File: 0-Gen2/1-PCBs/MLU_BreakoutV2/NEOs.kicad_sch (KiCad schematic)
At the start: 36 parts

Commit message: [add] beginning routing
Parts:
- renumbered LED5 to LED1
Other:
- note added: "first two are indicators, the remaining should be on breathe mode"
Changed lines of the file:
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@@
 		)
 	)
+	(text "first two are indicators, the remaining should be on breathe mode"
+		(exclude_from_sim no)
+		(at 16.764 14.478 0)
+		(effects
+			(font
+				(size 1.27 1.27)
+			)
+			(justify left)
+		)
+	)
 	(global_label "NEO_PASS5"
 		(shape output)
@@
 		(dnp no)
 		(fields_autoplaced yes)
-		(property "Reference" "LED5"
+		(property "Reference" "LED1"
 			(at 61.976 16.764 0)
 			(effects
@@
 			)
 		)
+		(property "MFR" ""
+			(at 41.656 26.67 0)
+			(effects
+				(font
+					(size 1.27 1.27)
+				)
+				(hide yes)
+			)
+		)
+		(property "MFR S/N" ""
+			(at 41.656 26.67 0)
+			(effects
+				(font
+					(size 1.27 1.27)
+				)
+				(hide yes)
+			)
+		)
+		(property "Supplier 1" ""
+			(at 41.656 26.67 0)
+			(effects
+				(font
+					(size 1.27 1.27)
+				)
+				(hide yes)
+			)
+		)
+		(property "Supplier 1 S/N" ""
+			(at 41.656 26.67 0)
+			(effects
+				(font
+					(size 1.27 1.27)
+				)
+				(hide yes)
+			)
+		)
+		(property "Supplier 2" ""
+			(at 41.656 26.67 0)
+			(effects
+				(font
+					(size 1.27 1.27)
+				)
+				(hide yes)
+			)
+		)
+		(property "Supplier 2 S/N" ""
+			(at 41.656 26.67 0)
+			(effects
+				(font
+					(size 1.27 1.27)
+				)
+				(hide yes)
+			)
+		)
 		(pin "3"
 		)
@@
 			(project "MLU_BreakoutV2"
 				(path "/55121ba7-5d22-4fe3-93aa-7f76d75b410c/38ea1217-5551-41b6-a3b9-444cd4c6916d"
-					(reference "LED5")
+					(reference "LED1")
 					(unit 1)
 				)

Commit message: before restructure
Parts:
- renumbered LED1 to LED5

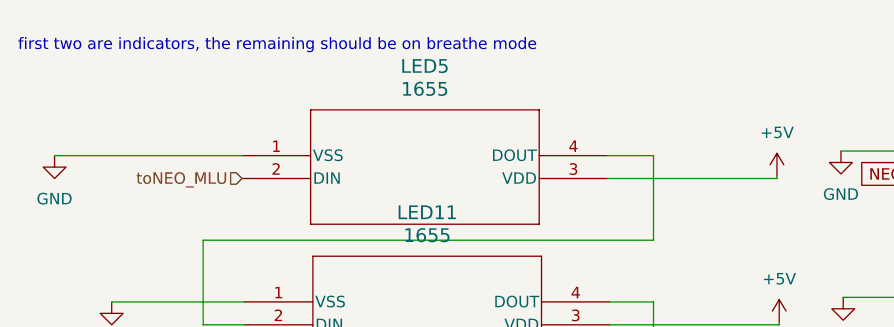
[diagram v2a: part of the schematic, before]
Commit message: [bugfix] rescued footprints
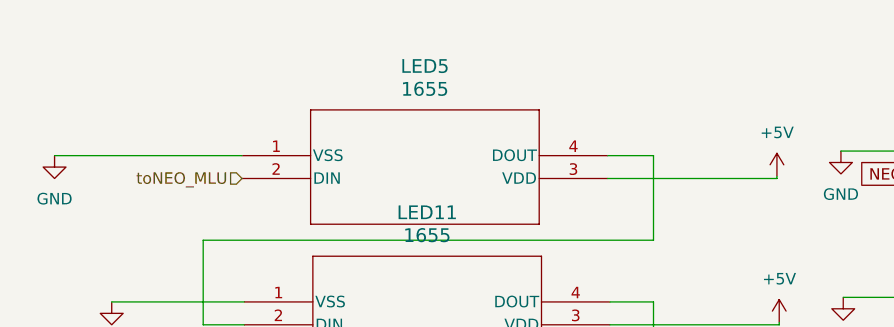
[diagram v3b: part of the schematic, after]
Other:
- note removed: "first two are indicators, the remaining should be on breathe mode"
